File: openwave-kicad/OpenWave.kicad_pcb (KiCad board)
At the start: 2 copper layers, 51 parts, among them IC1 STM32F405RGT, J1 USB_OTG, J2 503182-1852, J3 Screw_Terminal_01x04, J4 Conn_01x04_Female, U1 MIC5239-3.3YS, U2 MIC5209-4.2, U3 BNO055, U4 MAX3232, Y1 8MHz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

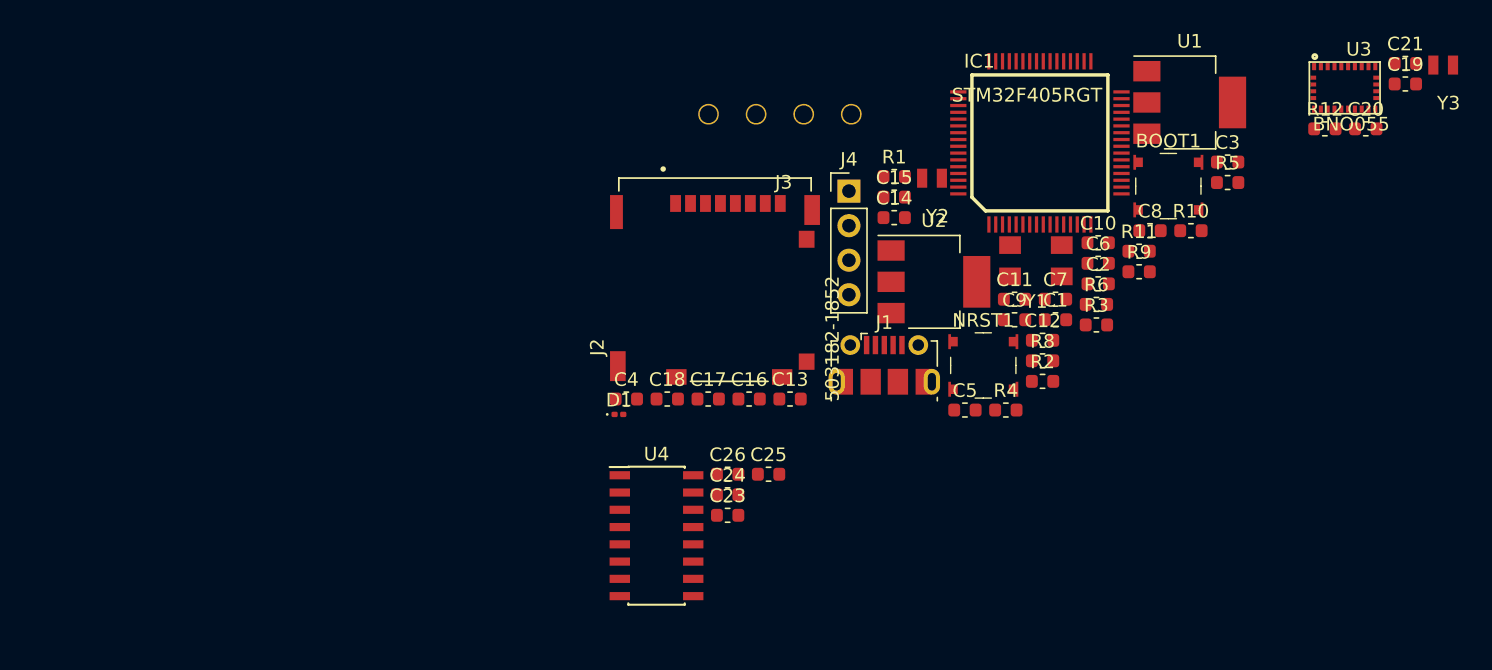
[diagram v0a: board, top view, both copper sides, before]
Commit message: fixed unconnected nets, routing 15% done
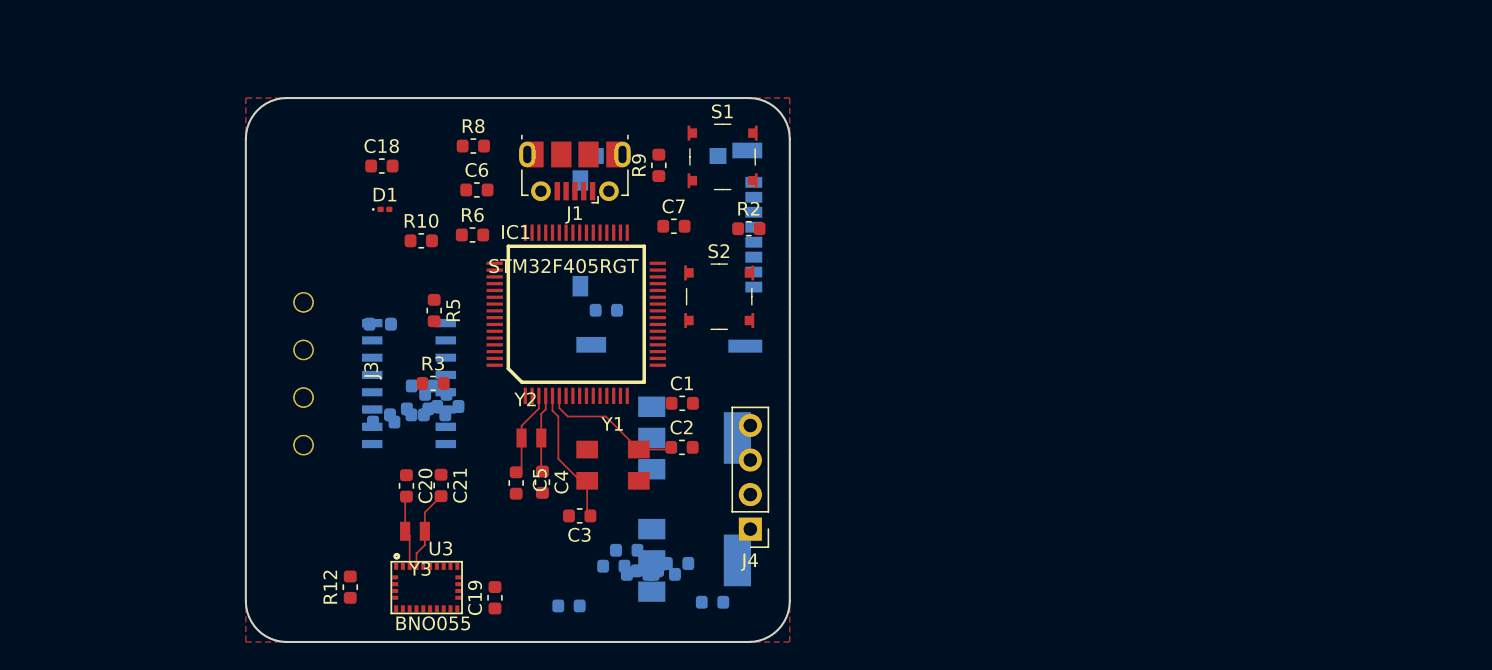
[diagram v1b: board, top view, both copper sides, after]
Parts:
- removed BOOT1, NRST1: SW_Push, digikey-footprints:Switch_Tactile_SMD_4.5x4.5mm_TL3315NF160Q
- added S1: TL3315NF160Q, digikey-footprints:Switch_Tactile_SMD_4.5x4.5mm_TL3315NF160Q, F.Cu at (99.1, 68.3)
- added S2: TL3315NF160Q, digikey-footprints:Switch_Tactile_SMD_4.5x4.5mm_TL3315NF160Q, F.Cu at (98.8, 78.6)
- C10, C11, C12, C13, C14, C15, C16, C17, C23, C24, C25, C26, C8, C9, J2, R1, R11, R4, U1, U2, U4: moved to B.Cu
- moved Y3 83.0 mm to (76.4, 95.9)
- moved R12 79.2 mm to (71.7, 100.0), turned to 90 degrees
- moved C21 77.4 mm to (78.4, 92.5), turned to 270 degrees
- moved C19 76.9 mm to (82.3, 100.8), turned to 90 degrees
- moved U3 76.9 mm to (77.3, 100.0)
- moved C20 75.3 mm to (75.8, 92.5), turned to 270 degrees
- moved R5 59.1 mm to (77.8, 79.6), turned to 270 degrees
- moved R10 56.6 mm to (76.9, 74.5)
- moved C3 54.3 mm to (88.5, 94.7), turned to 180 degrees
- moved R11 53.2 mm to (77.9, 87.3)
- moved J3 52.7 mm to (64.0, 72.0), turned to 90 degrees
- moved U1 49.6 mm to (97.0, 98.0)
- moved C10 49.3 mm to (78.8, 86.7)
- moved R3 49.0 mm to (77.8, 85.0)
- moved R6 46.2 mm to (80.7, 74.1)
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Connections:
- J4 pad 3: /TX2 -> /IO_PB10
- J4 pad 4: /RX2 -> /IO_PB11
- U4 pad 11: /STM_TX3 -> /IO_PA2
- U4 pad 12: /STM_RX3 -> /IO_PA3
- Y2 pad 2: Net-(Y2-Pad2) -> /N$5
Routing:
- net /N$9: track 0.00 -> 10.5 mm
- net /N$10: track 0.00 -> 10.3 mm
- net /N$5: track 0.00 -> 6.32 mm
- net /BNO055/XOUT32: track 0.00 -> 5.91 mm
- net /N$6: track 0.00 -> 5.73 mm
- net /BNO055/XIN32: track 0.00 -> 5.31 mm
- added copper zone on F.Cu, net GND
- added copper zone on GND, net GND
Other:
- board outline added: 40 x 40 mm
- copper layers 2 -> 4
- net class Default: clearance 0.2 -> 0.127
- rule trace_clearance: 0.2 -> 0.127
- rule trace_min: 0.2 -> 0.127
- rule via_min_drill: 0.3 -> 0.254

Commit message: routing ...51 connections left
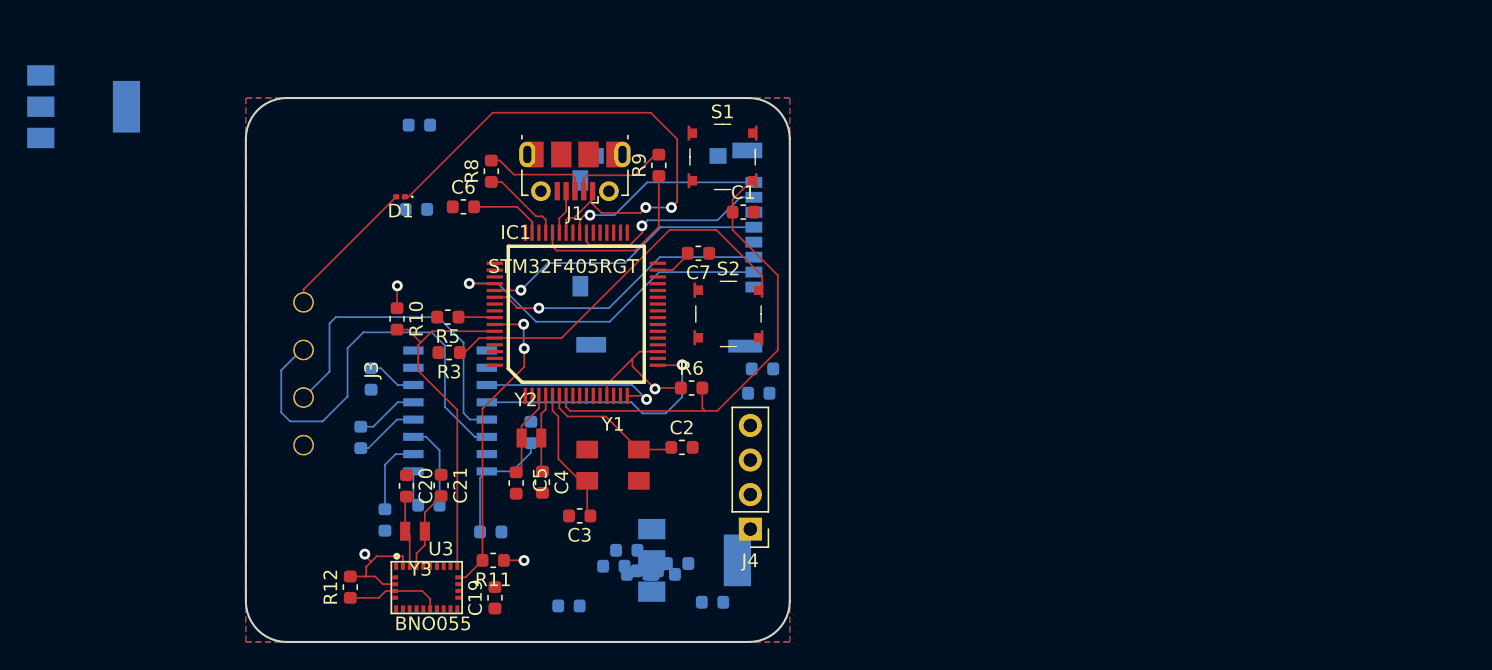
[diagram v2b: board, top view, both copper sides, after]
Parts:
- C18, R2: moved to B.Cu
- R11: moved to F.Cu
- moved U2 51.1 mm to (52.1, 64.6)
- moved C18 32.4 mm to (101.7, 85.7)
- moved R2 25.4 mm to (76.8, 66.0)
- moved R6 19.6 mm to (96.8, 85.3)
- moved C1 14.8 mm to (100.6, 72.4)
- moved C14 14.7 mm to (76.5, 72.2)
- moved R1 12.3 mm to (102.0, 83.9)
- moved R11 11.5 mm to (82.2, 98.0), turned to 180 degrees
- moved C10 9.76 mm to (82.0, 95.9)
- moved C24 8.45 mm to (72.5, 89.0), turned to 90 degrees
- moved C25 7.82 mm to (74.2, 95.0), turned to 90 degrees
- moved C15 7.53 mm to (85.0, 88.6), turned to 90 degrees
- moved C23 6.95 mm to (77.5, 93.9)
- moved R10 6.01 mm to (75.1, 80.2), turned to 270 degrees
- moved C26 3.81 mm to (73.2, 84.7), turned to 90 degrees
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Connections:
- C18 pad 1: Net-(C18-Pad1) -> /4.2V
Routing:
- net +5V: track 0.00 -> 39.2 mm, vias 0 -> 2
- net /NRST: track 0.00 -> 34.6 mm
- net +3V3: track 0.00 -> 31.6 mm, vias 0 -> 4
- net /RS232_TX: track 0.00 -> 31.4 mm
- net /BOOT0: track 0.00 -> 28.4 mm
- net /I2C1-SDA: track 0.00 -> 25.6 mm
- net /SDIO_D3: track 0.00 -> 25.5 mm, vias 0 -> 1
- net /RS232_RX: track 0.00 -> 24.2 mm
- net /I2C1-SCK: track 0.00 -> 23.1 mm, vias 0 -> 2
- net /SDIO_CMD: track 0.00 -> 21.0 mm, vias 0 -> 1
- net /SDIO_CK: track 0.00 -> 21.0 mm, vias 0 -> 1
- net /IO_PA3: track 0.00 -> 19.4 mm, vias 0 -> 1
- net /SDIO_D1: track 0.00 -> 14.9 mm, vias 0 -> 1
- net /SDIO_D0: track 0.00 -> 14.8 mm, vias 0 -> 1
- net /IO_PA2: track 0.00 -> 13.7 mm, vias 0 -> 1
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- added copper zone on B.Cu, net GND

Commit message: routing finished
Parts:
- C11, C9, R1: moved to F.Cu
- moved C17 34.8 mm to (68.9, 71.3), turned to 270 degrees
- moved C8 30.0 mm to (72.4, 77.4), turned to 90 degrees
- moved C11 26.1 mm to (78.4, 77.0)
- moved U2 25.5 mm to (76.7, 71.5)
- moved C9 22.1 mm to (71.1, 94.8)
- moved C1 20.6 mm to (96.8, 92.7), turned to 180 degrees
- moved C18 14.2 mm to (98.8, 99.6), turned to 180 degrees
- moved R2 11.5 mm to (83.9, 75.0), turned to 90 degrees
- moved R4 10.4 mm to (93.1, 88.7)
- moved C12 9.09 mm to (82.0, 97.8)
- moved C16 7.73 mm to (90.7, 99.9), turned to 270 degrees
- moved C13 7.53 mm to (88.4, 99.9), turned to 270 degrees
- moved C14 7.09 mm to (78.4, 79.0)
- moved U1 6.01 mm to (92.5, 94.1)
- moved R1 2.52 mm to (99.5, 83.7)
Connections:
- J4 pad 3: /IO_PB10 -> /IO_PB11
- J4 pad 4: /IO_PB11 -> /IO_PB10
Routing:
- net /4.2V: track 0.00 -> 89.1 mm, vias 0 -> 2
- net +3V3: track 31.6 -> 103.6 mm, vias 4 -> 6
- net +12V: track 10.6 -> 69.2 mm
- net /SDIO_D2: track 0.00 -> 31.7 mm, vias 0 -> 1
- net /IO_PB11: track 0.00 -> 27.9 mm, vias 0 -> 1
- net Net-(J1-Pad6): track 0.00 -> 19.0 mm
- net /IO_PB10: track 0.00 -> 14.4 mm, vias 0 -> 1
- net GND: track 0.00 -> 8.68 mm, vias 0 -> 6
- net /IO_PB2: track 0.00 -> 8.48 mm
- net Net-(C19-Pad1): track 0.00 -> 7.03 mm
- net /NRST: track 34.6 -> 41.1 mm
- net /SDIO_D3: track 25.5 -> 27.8 mm
- net Net-(R12-Pad1): track 7.06 -> 8.20 mm
- net /I2C1-SCK: track 23.1 -> 22.6 mm
- added copper zone on POWER, net +3V3

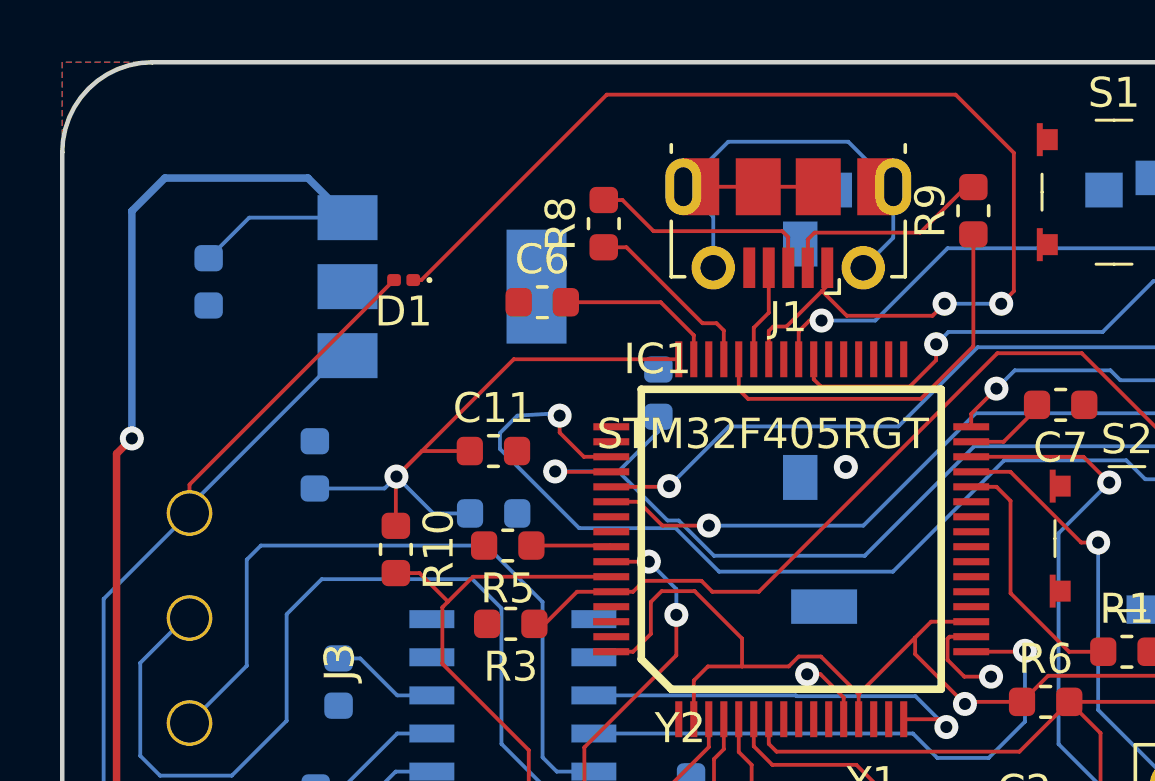
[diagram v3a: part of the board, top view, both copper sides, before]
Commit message: replaced incorrect usb connector
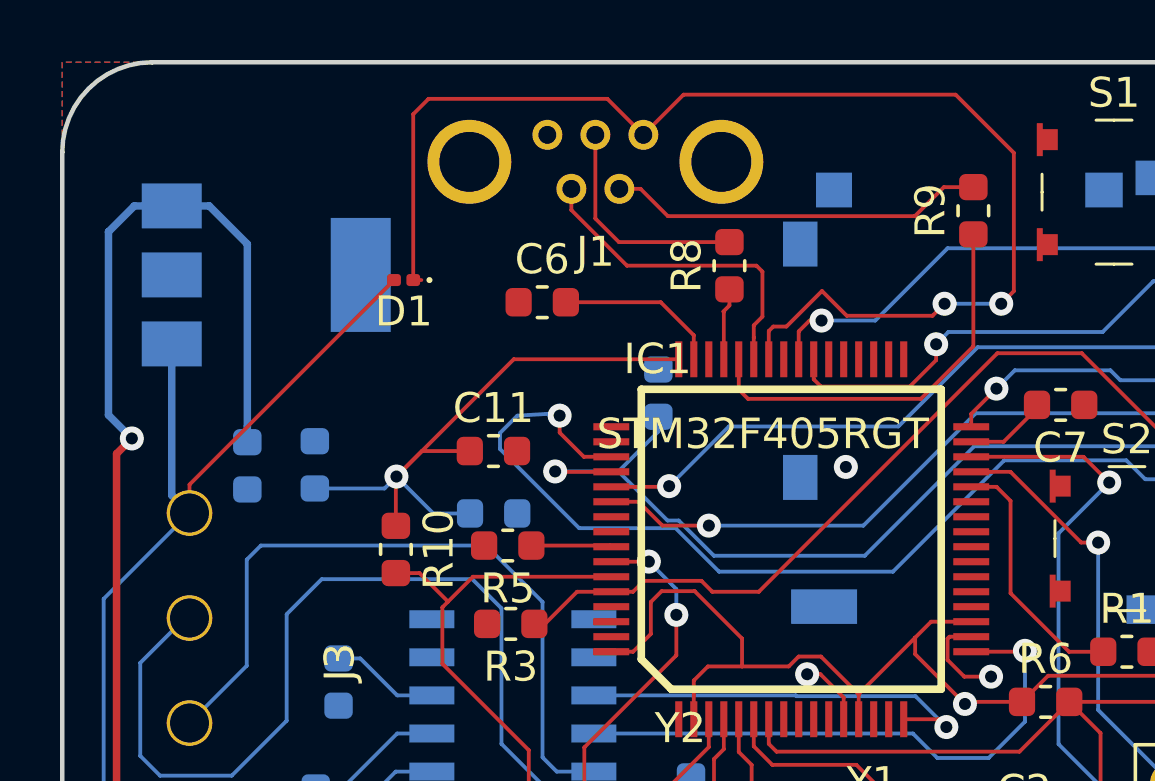
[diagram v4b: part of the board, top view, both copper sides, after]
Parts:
- J1: footprint my_footprints:USB_Micro-B_Molex-105017-0001 -> my_footprints:wurth_usb_connector
- moved J1 6.76 mm to (81.8, 66.4), turned to 0 degrees
- moved C17 6.27 mm to (70.2, 77.5)
- moved U2 5.87 mm to (70.8, 71.1)
- moved R8 4.42 mm to (86.2, 70.8)
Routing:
- net Net-(J1-Pad6): track 19.0 -> 0.00 mm
- net /FS_USB_ID: track 3.26 -> 11.0 mm
- net Net-(J1-Pad2): track 7.18 -> 12.8 mm
- net /FS_DP: track 6.11 -> 2.42 mm
- net +5V: track 39.2 -> 42.8 mm
- net +12V: track 69.2 -> 67.5 mm
- net /4.2V: track 89.1 -> 87.5 mm

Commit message: added openwave to front silk
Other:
- board text added: "BOOT"
- board text added: "OpenWave"
- board text added: "RST"
- board text added: "v0.1"
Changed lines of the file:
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@@
   (general
     (thickness 1.6)
-    (drawings 8)
+    (drawings 12)
     (tracks 428)
     (zones 0)
@@
   (page A4)
   (layers
-    (0 F.Cu signal)
+    (0 F.Cu signal hide)
     (1 GND signal hide)
     (2 POWER signal hide)
@@
     (solder_mask_min_width 0.25)
     (aux_axis_origin 0 0)
-    (visible_elements FFFFFFFF)
+    (visible_elements FFFEFBFF)
     (pcbplotparams
       (layerselection 0x010fc_ffffffff)
@@
     (pad 7 thru_hole circle (at -4.2 0.9) (size 2.8 2.8) (drill 2) (layers *.Cu *.Mask))
   )
+  (gr_text v0.1 (at 93.4 102.82) (layer F.SilkS)
+    (effects (font (size 1 1) (thickness 0.2)))
+  )
+  (gr_text OpenWave (at 93.66 100.17) (layer F.SilkS)
+    (effects (font (size 2.7 2.7) (thickness 0.3) italic))
+  )
+  (gr_text BOOT (at 103.01 80.03 90) (layer F.SilkS)
+    (effects (font (size 1 1) (thickness 0.2)))
+  )
+  (gr_text RST (at 102.78 68.53 90) (layer F.SilkS)
+    (effects (font (size 1 1) (thickness 0.2)))
+  )
   (gr_line (start 101 64) (end 67 64) (angle 90) (layer Edge.Cuts) (width 0.15))
